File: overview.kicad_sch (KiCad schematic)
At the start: 0 parts

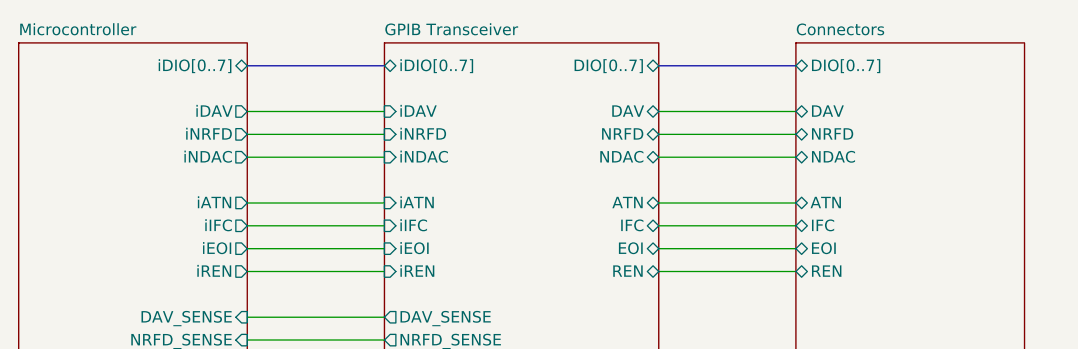
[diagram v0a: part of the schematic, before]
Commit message: Fix GPIB DIO bus nets and start PCB. Adjusted to 4 layers
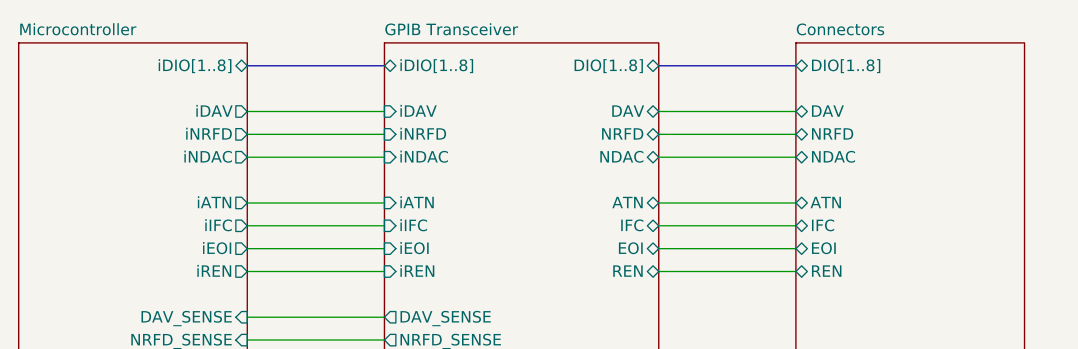
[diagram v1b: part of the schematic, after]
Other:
- sheet Connectors ports: added DIO[1..8]; removed DIO[0..7]
- sheet GPIB Transceiver ports: added DIO[1..8], iDIO[1..8]; removed DIO[0..7], iDIO[0..7]
- sheet Microcontroller ports: added iDIO[1..8]; removed iDIO[0..7]
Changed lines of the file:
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@@
-			)
-		)
-		(pin "iDIO[0..7]" bidirectional
-			(at 195.58 88.9 180)
-			(effects
-				(font
-					(size 1.27 1.27)
-				)
-				(justify left)
-			)
-		)
-		(pin "DIO[0..7]" bidirectional
-			(at 226.06 88.9 0)
-			(effects
-				(font
-					(size 1.27 1.27)
-				)
-				(justify right)
 			)
 		)
@@
 				)
 				(justify left)
+			)
+		)
+		(pin "iDIO[1..8]" bidirectional
+			(at 195.58 88.9 180)
+			(effects
+				(font
+					(size 1.27 1.27)
+				)
+				(justify left)
+			)
+		)
+		(pin "DIO[1..8]" bidirectional
+			(at 226.06 88.9 0)
+			(effects
+				(font
+					(size 1.27 1.27)
+				)
+				(justify right)
 			)
 		)
@@
 			)
 		)
-		(pin "iDIO[0..7]" bidirectional
-			(at 180.34 88.9 0)
-			(effects
-				(font
-					(size 1.27 1.27)
-				)
-				(justify right)
-			)
-		)
 		(pin "iEOI" output
 			(at 180.34 109.22 0)
@@
 		(pin "GPIB_DIR" output
 			(at 180.34 134.62 0)
+			(effects
+				(font
+					(size 1.27 1.27)
+				)
+				(justify right)
+			)
+		)
+		(pin "iDIO[1..8]" bidirectional
+			(at 180.34 88.9 0)
 			(effects
 				(font
@@
 			)
 		)
-		(pin "DIO[0..7]" bidirectional
-			(at 241.3 88.9 180)
-			(effects
-				(font
-					(size 1.27 1.27)
-				)
-				(justify left)
-			)
-		)
 		(pin "CTRL_RX_N" bidirectional
 			(at 241.3 157.48 180)
@@
 			(effects
 				(font
+					(size 1.27 1.27)
+				)
+				(justify left)
+			)
+		)
+		(pin "DIO[1..8]" bidirectional
+			(at 241.3 88.9 180)
+			(effects
+				(font

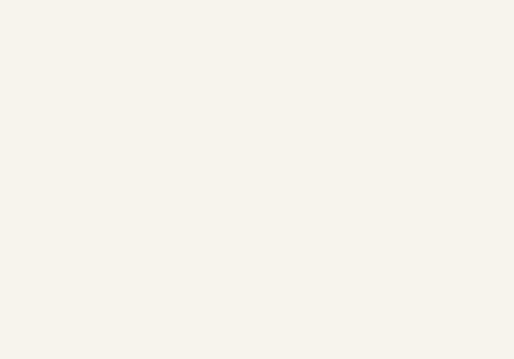
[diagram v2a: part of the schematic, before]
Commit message: Change board size, complete bottom routing, update (still broken) jobfile
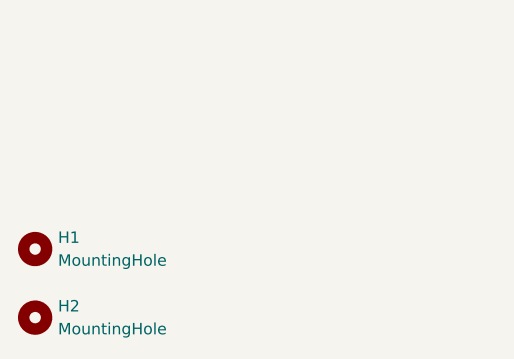
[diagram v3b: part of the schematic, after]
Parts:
- added H1, H2: MountingHole, MountingHole:MountingHole_2.1mm, symbol Mechanical:MountingHole
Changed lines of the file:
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@@
+		)
+	)
+	(symbol
+		(lib_id "Mechanical:MountingHole")
+		(at 63.5 200.66 0)
+		(unit 1)
+		(body_style 1)
+		(exclude_from_sim no)
+		(in_bom no)
+		(on_board yes)
+		(in_pos_files yes)
+		(dnp no)
+		(fields_autoplaced yes)
+		(property "Reference" "H2"
+			(at 66.04 199.39 0)
+			(show_name no)
+			(do_not_autoplace no)
+			(effects
+				(font
+					(size 1.27 1.27)
+				)
+				(justify left)
+			)
+		)
+		(property "Value" "MountingHole"
+			(at 66.04 201.93 0)
+			(show_name no)
+			(do_not_autoplace no)
+			(effects
+				(font
+					(size 1.27 1.27)
+				)
+				(justify left)
+			)
+		)
+		(property "Footprint" "MountingHole:MountingHole_2.1mm"
+			(at 63.5 200.66 0)
+			(hide yes)
+			(show_name no)
+			(do_not_autoplace no)
+			(effects
+				(font
+					(size 1.27 1.27)
+				)
+			)
+		)
+		(property "Datasheet" ""
+			(at 63.5 200.66 0)
+			(hide yes)
+			(show_name no)
+			(do_not_autoplace no)
+			(effects
+				(font
+					(size 1.27 1.27)
+				)
+			)
+		)
+		(property "Description" "Mounting Hole without connection"
+			(at 63.5 200.66 0)
+			(hide yes)
+			(show_name no)
+			(do_not_autoplace no)
+			(effects
+				(font
+					(size 1.27 1.27)
+				)
+			)
+		)
+		(instances
+			(project "gpib_controller"
+				(path "/0f352524-50ff-469d-9a68-783e183b0073/642cbd6b-8c2c-4a8a-b65c-89c798f24c3f"
+					(reference "H2")
+					(unit 1)
+				)
+			)
+		)
+	)
+	(symbol
+		(lib_id "Mechanical:MountingHole")
+		(at 63.5 193.04 0)
+		(unit 1)
+		(body_style 1)
+		(exclude_from_sim no)
+		(in_bom no)
+		(on_board yes)
+		(in_pos_files yes)
+		(dnp no)
+		(fields_autoplaced yes)
+		(property "Reference" "H1"
+			(at 66.04 191.77 0)
+			(show_name no)
+			(do_not_autoplace no)
+			(effects
+				(font
+					(size 1.27 1.27)
+				)
+				(justify left)
+			)
+		)
+		(property "Value" "MountingHole"
+			(at 66.04 194.31 0)
+			(show_name no)
+			(do_not_autoplace no)
+			(effects
+				(font
+					(size 1.27 1.27)
+				)
+				(justify left)
+			)
+		)
+		(property "Footprint" "MountingHole:MountingHole_2.1mm"
+			(at 63.5 193.04 0)
+			(hide yes)
+			(show_name no)
+			(do_not_autoplace no)
+			(effects
+				(font
+					(size 1.27 1.27)
+				)
+			)
+		)
+		(property "Datasheet" ""
+			(at 63.5 193.04 0)
+			(hide yes)
+			(show_name no)
+			(do_not_autoplace no)
+			(effects
+				(font
+					(size 1.27 1.27)
+				)
+			)
+		)
+		(property "Description" "Mounting Hole without connection"
+			(at 63.5 193.04 0)
+			(hide yes)
+			(show_name no)
+			(do_not_autoplace no)
+			(effects
+				(font
+					(size 1.27 1.27)
+				)
+			)
+		)
+		(instances
+			(project "gpib_controller"
+				(path "/0f352524-50ff-469d-9a68-783e183b0073/642cbd6b-8c2c-4a8a-b65c-89c798f24c3f"
+					(reference "H1")
+					(unit 1)
+				)
+			)
 		)
 	)
